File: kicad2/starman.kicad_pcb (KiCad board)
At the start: 2 copper layers, 160 x 150 mm, 60 parts

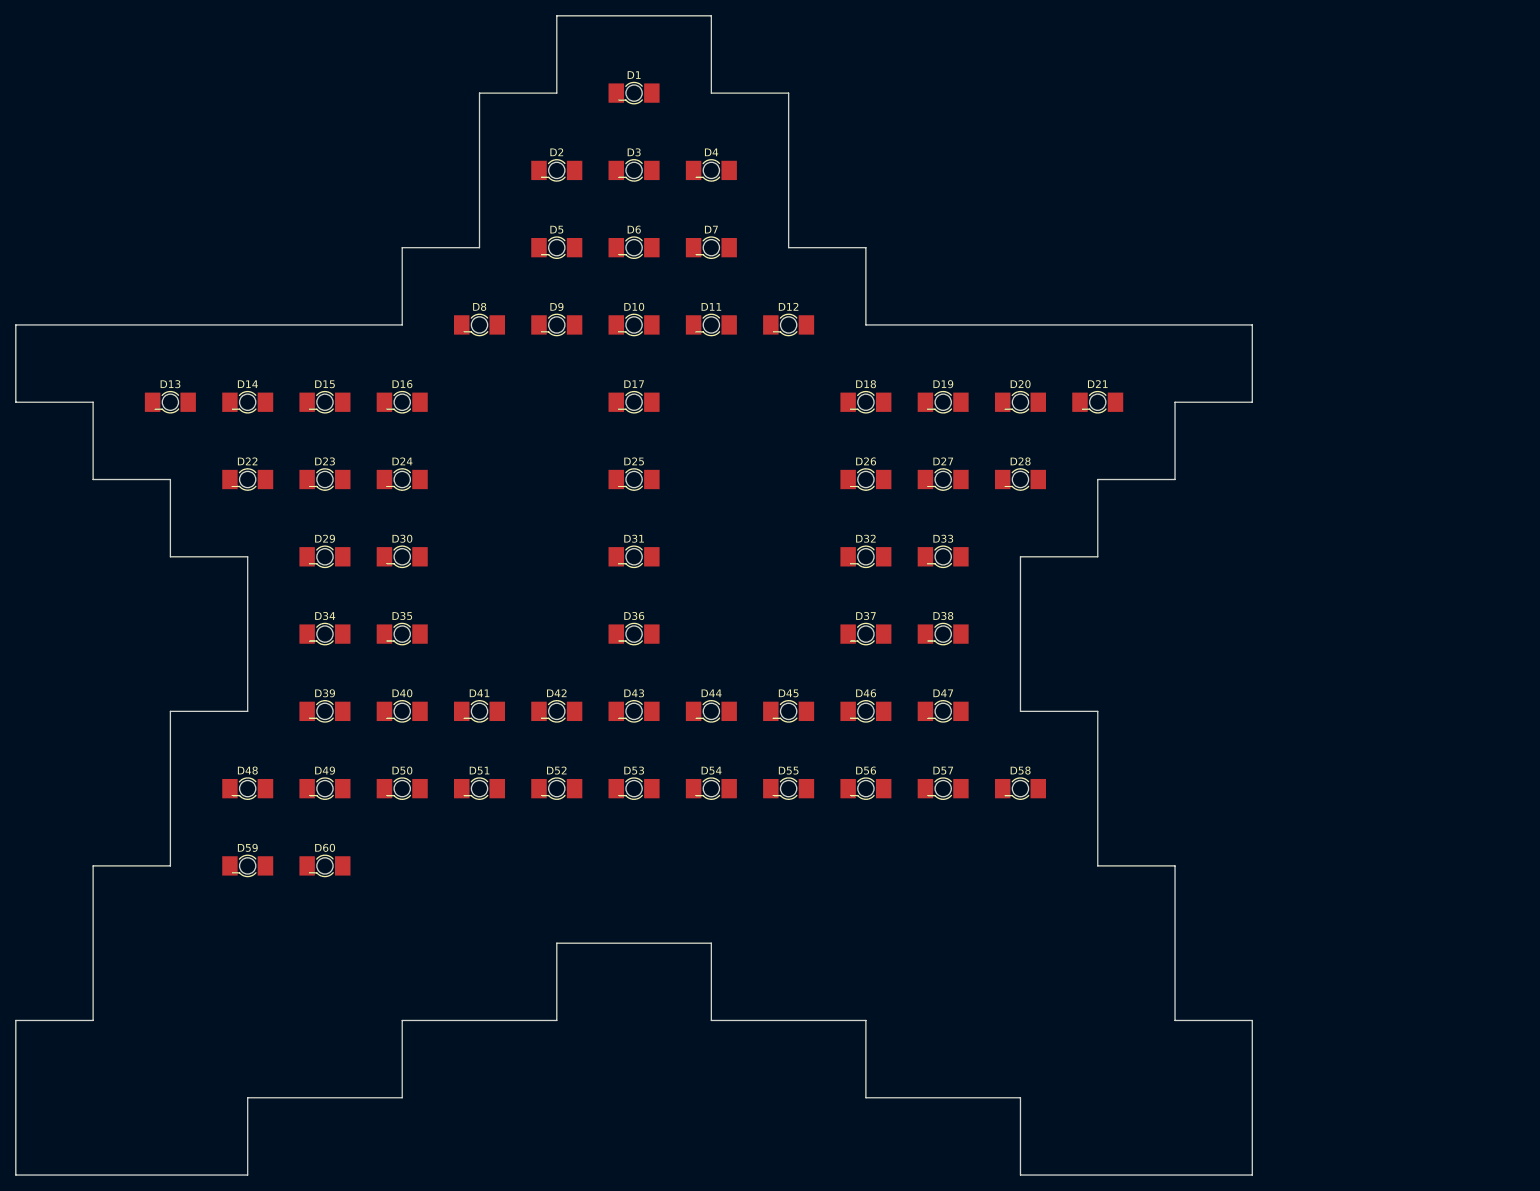
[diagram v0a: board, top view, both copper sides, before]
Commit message: Placements of components and things
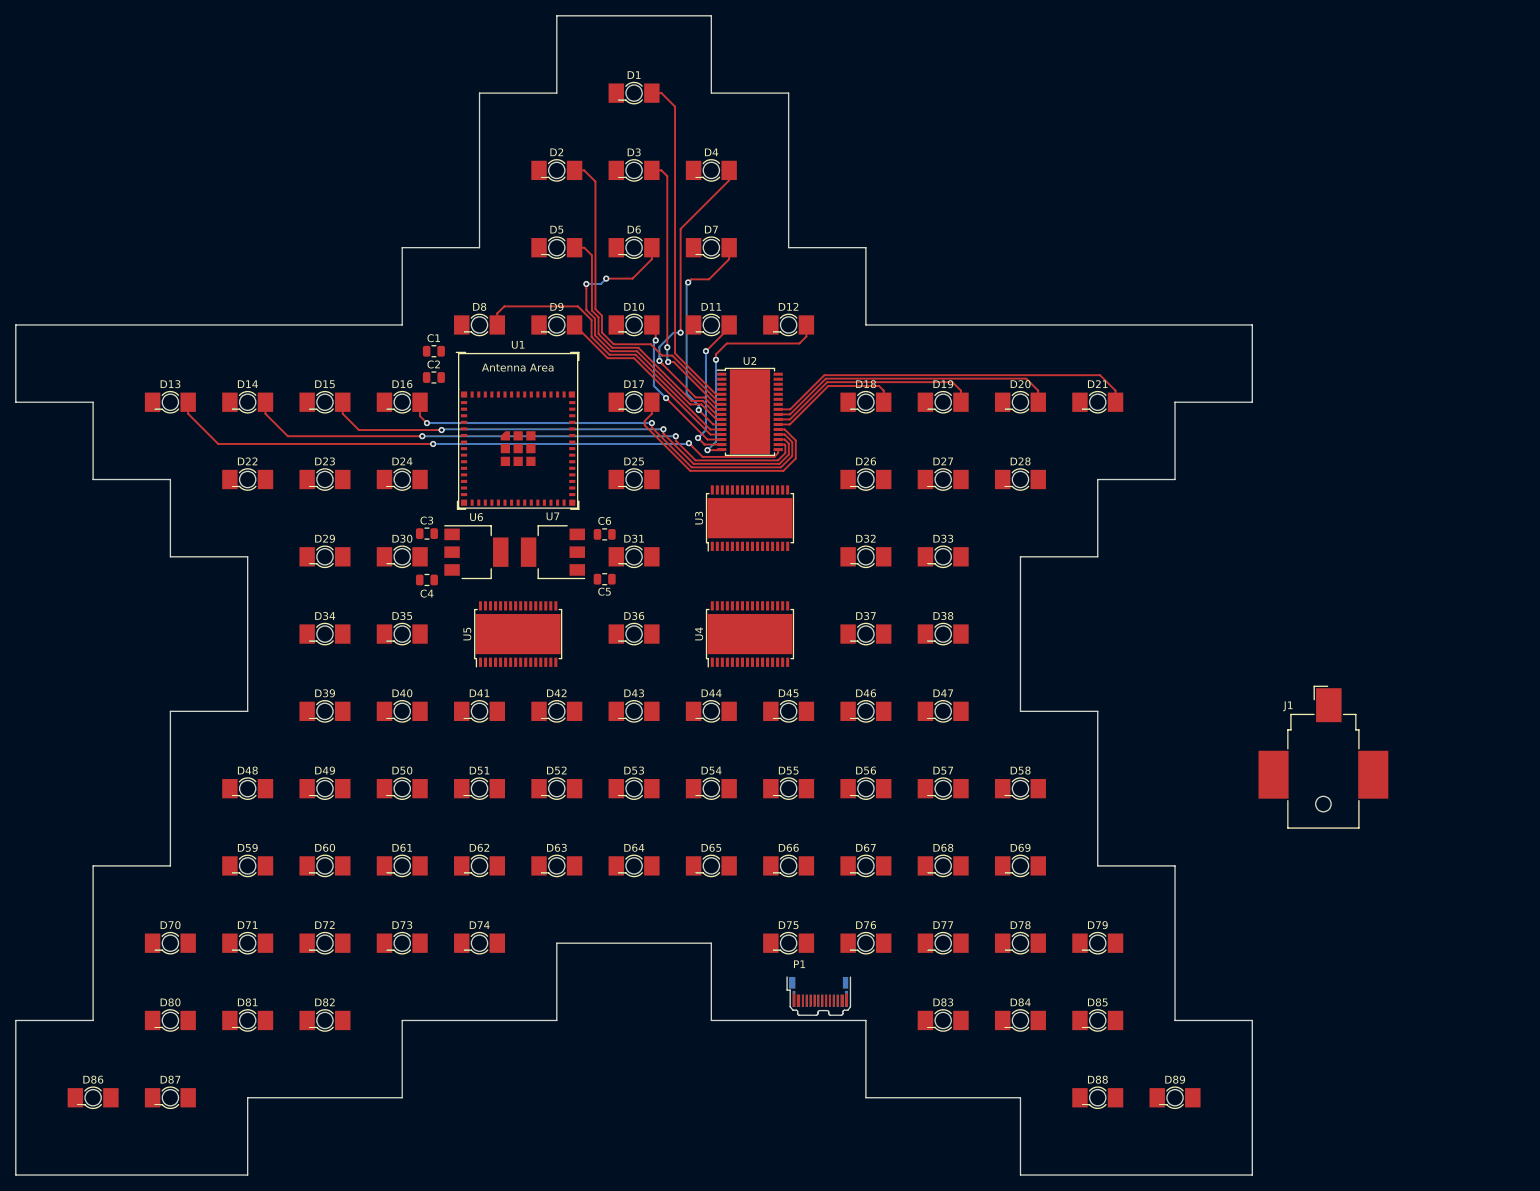
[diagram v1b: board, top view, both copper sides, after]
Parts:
- added C1: C, Capacitor_SMD:C_0805_2012Metric, F.Cu at (84.1, 73.4)
- added C2: C, Capacitor_SMD:C_0805_2012Metric, F.Cu at (84.1, 76.8)
- added C3: C, Capacitor_SMD:C_0805_2012Metric, F.Cu at (83.2, 97.0)
- added C4: C, Capacitor_SMD:C_0805_2012Metric, F.Cu at (83.2, 103.0)
- added C5: C, Capacitor_SMD:C_0805_2012Metric, F.Cu at (106.2, 102.9)
- added C6: C, Capacitor_SMD:C_0805_2012Metric, F.Cu at (106.2, 97.1)
- added D61: LED, LED_SMD:LED_Osram_Lx_P47F_D2mm_ReverseMount, F.Cu at (80.0, 140.0)
- added D62: LED, LED_SMD:LED_Osram_Lx_P47F_D2mm_ReverseMount, F.Cu at (90.0, 140.0)
- added D63: LED, LED_SMD:LED_Osram_Lx_P47F_D2mm_ReverseMount, F.Cu at (100.0, 140.0)
- added D64: LED, LED_SMD:LED_Osram_Lx_P47F_D2mm_ReverseMount, F.Cu at (110.0, 140.0)
- added D65: LED, LED_SMD:LED_Osram_Lx_P47F_D2mm_ReverseMount, F.Cu at (120.0, 140.0)
- added D66: LED, LED_SMD:LED_Osram_Lx_P47F_D2mm_ReverseMount, F.Cu at (130.0, 140.0)
- added D67: LED, LED_SMD:LED_Osram_Lx_P47F_D2mm_ReverseMount, F.Cu at (140.0, 140.0)
- added D68: LED, LED_SMD:LED_Osram_Lx_P47F_D2mm_ReverseMount, F.Cu at (150.0, 140.0)
- added D69: LED, LED_SMD:LED_Osram_Lx_P47F_D2mm_ReverseMount, F.Cu at (160.0, 140.0)
- added D70: LED, LED_SMD:LED_Osram_Lx_P47F_D2mm_ReverseMount, F.Cu at (50.0, 150.0)
- added D71: LED, LED_SMD:LED_Osram_Lx_P47F_D2mm_ReverseMount, F.Cu at (60.0, 150.0)
- added D72: LED, LED_SMD:LED_Osram_Lx_P47F_D2mm_ReverseMount, F.Cu at (70.0, 150.0)
- added D73: LED, LED_SMD:LED_Osram_Lx_P47F_D2mm_ReverseMount, F.Cu at (80.0, 150.0)
- added D74: LED, LED_SMD:LED_Osram_Lx_P47F_D2mm_ReverseMount, F.Cu at (90.0, 150.0)
- added D75: LED, LED_SMD:LED_Osram_Lx_P47F_D2mm_ReverseMount, F.Cu at (130.0, 150.0)
- added D76: LED, LED_SMD:LED_Osram_Lx_P47F_D2mm_ReverseMount, F.Cu at (140.0, 150.0)
- added D77: LED, LED_SMD:LED_Osram_Lx_P47F_D2mm_ReverseMount, F.Cu at (150.0, 150.0)
- added D78: LED, LED_SMD:LED_Osram_Lx_P47F_D2mm_ReverseMount, F.Cu at (160.0, 150.0)
- added D79: LED, LED_SMD:LED_Osram_Lx_P47F_D2mm_ReverseMount, F.Cu at (170.0, 150.0)
- added D80: LED, LED_SMD:LED_Osram_Lx_P47F_D2mm_ReverseMount, F.Cu at (50.0, 160.0)
- added D81: LED, LED_SMD:LED_Osram_Lx_P47F_D2mm_ReverseMount, F.Cu at (60.0, 160.0)
- added D82: LED, LED_SMD:LED_Osram_Lx_P47F_D2mm_ReverseMount, F.Cu at (70.0, 160.0)
- added D83: LED, LED_SMD:LED_Osram_Lx_P47F_D2mm_ReverseMount, F.Cu at (150.0, 160.0)
- added D84: LED, LED_SMD:LED_Osram_Lx_P47F_D2mm_ReverseMount, F.Cu at (160.0, 160.0)
- added D85: LED, LED_SMD:LED_Osram_Lx_P47F_D2mm_ReverseMount, F.Cu at (170.0, 160.0)
- added D86: LED, LED_SMD:LED_Osram_Lx_P47F_D2mm_ReverseMount, F.Cu at (40.0, 170.0)
- added D87: LED, LED_SMD:LED_Osram_Lx_P47F_D2mm_ReverseMount, F.Cu at (50.0, 170.0)
- added D88: LED, LED_SMD:LED_Osram_Lx_P47F_D2mm_ReverseMount, F.Cu at (170.0, 170.0)
- added D89: LED, LED_SMD:LED_Osram_Lx_P47F_D2mm_ReverseMount, F.Cu at (180.0, 170.0)
- added J1: Barrel_Jack, Connector_BarrelJack:BarrelJack_CUI_PJ-036AH-SMT_Horizontal, F.Cu at (199.2, 125.0)
- added P1: USB_C_Plug_USB2.0, Connector_USB:USB_C_Plug_JAE_DX07P024AJ1, F.Cu at (134.1, 156.3)
- added U1: ESP32-S2-MINI-1, Espressif:ESP32-S2-MINI-1, F.Cu at (95.0, 86.0)
- added U2: TLC5947DAP, Package_SO:HTSSOP-32-1EP_6.1x11mm_P0.65mm_EP5.2x11mm_Mask4.11x4.36mm, F.Cu at (125.0, 81.2)
- added U3: TLC5947DAP, Package_SO:HTSSOP-32-1EP_6.1x11mm_P0.65mm_EP5.2x11mm_Mask4.11x4.36mm, F.Cu at (125.0, 95.0)
- added U4: TLC5947DAP, Package_SO:HTSSOP-32-1EP_6.1x11mm_P0.65mm_EP5.2x11mm_Mask4.11x4.36mm, F.Cu at (125.0, 110.0)
- added U5: TLC5947DAP, Package_SO:HTSSOP-32-1EP_6.1x11mm_P0.65mm_EP5.2x11mm_Mask4.11x4.36mm, F.Cu at (95.0, 110.0)
- added U6: LF33_TO220, Package_TO_SOT_SMD:SOT-223, F.Cu at (89.6, 99.4)
- added U7: LF50_TO220, Package_TO_SOT_SMD:SOT-223, F.Cu at (99.5, 99.4)
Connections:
- D1 pad 1: (no net) -> GND
- D1 pad 2: (no net) -> Net-(D1-Pad2)
- D10 pad 1: (no net) -> GND
- D10 pad 2: (no net) -> Net-(D10-Pad2)
- D11 pad 1: (no net) -> GND
- D11 pad 2: (no net) -> Net-(D11-Pad2)
- D12 pad 1: (no net) -> GND
- D12 pad 2: (no net) -> Net-(D12-Pad2)
- D13 pad 1: (no net) -> GND
- D13 pad 2: (no net) -> Net-(D13-Pad2)
- D14 pad 1: (no net) -> GND
- D14 pad 2: (no net) -> Net-(D14-Pad2)
- D15 pad 1: (no net) -> GND
- D15 pad 2: (no net) -> Net-(D15-Pad2)
- D16 pad 1: (no net) -> GND
- D16 pad 2: (no net) -> Net-(D16-Pad2)
- D17 pad 1: (no net) -> GND
- D17 pad 2: (no net) -> Net-(D17-Pad2)
- D18 pad 1: (no net) -> GND
- D18 pad 2: (no net) -> Net-(D18-Pad2)
- D19 pad 1: (no net) -> GND
- D19 pad 2: (no net) -> Net-(D19-Pad2)
- D2 pad 1: (no net) -> GND
- D2 pad 2: (no net) -> Net-(D2-Pad2)
- D20 pad 1: (no net) -> GND
- D20 pad 2: (no net) -> Net-(D20-Pad2)
- D21 pad 1: (no net) -> GND
- D21 pad 2: (no net) -> Net-(D21-Pad2)
- D22 pad 1: (no net) -> GND
- D22 pad 2: (no net) -> Net-(D22-Pad2)
- D23 pad 1: (no net) -> GND
- D23 pad 2: (no net) -> Net-(D23-Pad2)
- D24 pad 1: (no net) -> GND
- D24 pad 2: (no net) -> Net-(D24-Pad2)
- D25 pad 1: (no net) -> GND
- D25 pad 2: (no net) -> Net-(D25-Pad2)
- D26 pad 1: (no net) -> GND
- D26 pad 2: (no net) -> Net-(D26-Pad2)
- D27 pad 1: (no net) -> GND
- D27 pad 2: (no net) -> Net-(D27-Pad2)
- D28 pad 1: (no net) -> GND
- D28 pad 2: (no net) -> Net-(D28-Pad2)
- D29 pad 1: (no net) -> GND
- D29 pad 2: (no net) -> Net-(D29-Pad2)
- D3 pad 1: (no net) -> GND
- D3 pad 2: (no net) -> Net-(D3-Pad2)
- D30 pad 1: (no net) -> GND
- D30 pad 2: (no net) -> Net-(D30-Pad2)
- D31 pad 1: (no net) -> GND
- D31 pad 2: (no net) -> Net-(D31-Pad2)
- D32 pad 1: (no net) -> GND
- D32 pad 2: (no net) -> Net-(D32-Pad2)
- D33 pad 1: (no net) -> GND
- D33 pad 2: (no net) -> Net-(D33-Pad2)
- D34 pad 1: (no net) -> GND
- D34 pad 2: (no net) -> Net-(D34-Pad2)
- D35 pad 1: (no net) -> GND
- D35 pad 2: (no net) -> Net-(D35-Pad2)
- D36 pad 1: (no net) -> GND
- D36 pad 2: (no net) -> Net-(D36-Pad2)
- D37 pad 1: (no net) -> GND
- D37 pad 2: (no net) -> Net-(D37-Pad2)
- D38 pad 1: (no net) -> GND
- D38 pad 2: (no net) -> Net-(D38-Pad2)
- D39 pad 1: (no net) -> GND
- D39 pad 2: (no net) -> Net-(D39-Pad2)
- D4 pad 1: (no net) -> GND
- D4 pad 2: (no net) -> Net-(D4-Pad2)
- D40 pad 1: (no net) -> GND
- D40 pad 2: (no net) -> Net-(D40-Pad2)
- D41 pad 1: (no net) -> GND
- D41 pad 2: (no net) -> Net-(D41-Pad2)
- D42 pad 1: (no net) -> GND
- D42 pad 2: (no net) -> Net-(D42-Pad2)
- D43 pad 1: (no net) -> GND
- D43 pad 2: (no net) -> Net-(D43-Pad2)
- D44 pad 1: (no net) -> GND
- D44 pad 2: (no net) -> Net-(D44-Pad2)
- D45 pad 1: (no net) -> GND
- D45 pad 2: (no net) -> Net-(D45-Pad2)
- D46 pad 1: (no net) -> GND
- D46 pad 2: (no net) -> Net-(D46-Pad2)
- D47 pad 1: (no net) -> GND
- D47 pad 2: (no net) -> Net-(D47-Pad2)
- D48 pad 1: (no net) -> GND
- D48 pad 2: (no net) -> Net-(D48-Pad2)
- D49 pad 1: (no net) -> GND
- D49 pad 2: (no net) -> Net-(D49-Pad2)
- D5 pad 1: (no net) -> GND
- D5 pad 2: (no net) -> Net-(D5-Pad2)
- D50 pad 1: (no net) -> GND
- D50 pad 2: (no net) -> Net-(D50-Pad2)
- D51 pad 1: (no net) -> GND
- D51 pad 2: (no net) -> Net-(D51-Pad2)
- D52 pad 1: (no net) -> GND
- D52 pad 2: (no net) -> Net-(D52-Pad2)
- D53 pad 1: (no net) -> GND
- D53 pad 2: (no net) -> Net-(D53-Pad2)
- D54 pad 1: (no net) -> GND
- D54 pad 2: (no net) -> Net-(D54-Pad2)
- D55 pad 1: (no net) -> GND
- D55 pad 2: (no net) -> Net-(D55-Pad2)
- D56 pad 1: (no net) -> GND
- D56 pad 2: (no net) -> Net-(D56-Pad2)
- D57 pad 1: (no net) -> GND
- D57 pad 2: (no net) -> Net-(D57-Pad2)
- D58 pad 1: (no net) -> GND
- D58 pad 2: (no net) -> Net-(D58-Pad2)
- D59 pad 1: (no net) -> GND
- D59 pad 2: (no net) -> Net-(D59-Pad2)
- D6 pad 1: (no net) -> GND
- D6 pad 2: (no net) -> Net-(D6-Pad2)
- D60 pad 1: (no net) -> GND
- D60 pad 2: (no net) -> Net-(D60-Pad2)
- D7 pad 1: (no net) -> GND
- D7 pad 2: (no net) -> Net-(D7-Pad2)
- D8 pad 1: (no net) -> GND
- D8 pad 2: (no net) -> Net-(D8-Pad2)
- D9 pad 1: (no net) -> GND
- D9 pad 2: (no net) -> Net-(D9-Pad2)
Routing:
- net Net-(D13-Pad2): track 0.00 -> 80.9 mm, vias 0 -> 2
- net Net-(D14-Pad2): track 0.00 -> 74.0 mm, vias 0 -> 2
- net Net-(D15-Pad2): track 0.00 -> 65.8 mm, vias 0 -> 2
- net Net-(D16-Pad2): track 0.00 -> 57.7 mm, vias 0 -> 2
- net Net-(D21-Pad2): track 0.00 -> 47.8 mm
- net Net-(D1-Pad2): track 0.00 -> 43.9 mm
- net Net-(D2-Pad2): track 0.00 -> 42.3 mm
- net Net-(D4-Pad2): track 0.00 -> 39.6 mm, vias 0 -> 2
- net Net-(D6-Pad2): track 0.00 -> 39.3 mm, vias 0 -> 2
- net Net-(D8-Pad2): track 0.00 -> 38.8 mm
- net Net-(D20-Pad2): track 0.00 -> 37.7 mm
- net Net-(D3-Pad2): track 0.00 -> 35.6 mm, vias 0 -> 2
- net Net-(D5-Pad2): track 0.00 -> 33.4 mm
- net Net-(D17-Pad2): track 0.00 -> 31.2 mm
- net Net-(D7-Pad2): track 0.00 -> 29.0 mm, vias 0 -> 2
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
